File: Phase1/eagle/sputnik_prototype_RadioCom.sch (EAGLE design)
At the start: 56 parts, among them Y1 32MHz

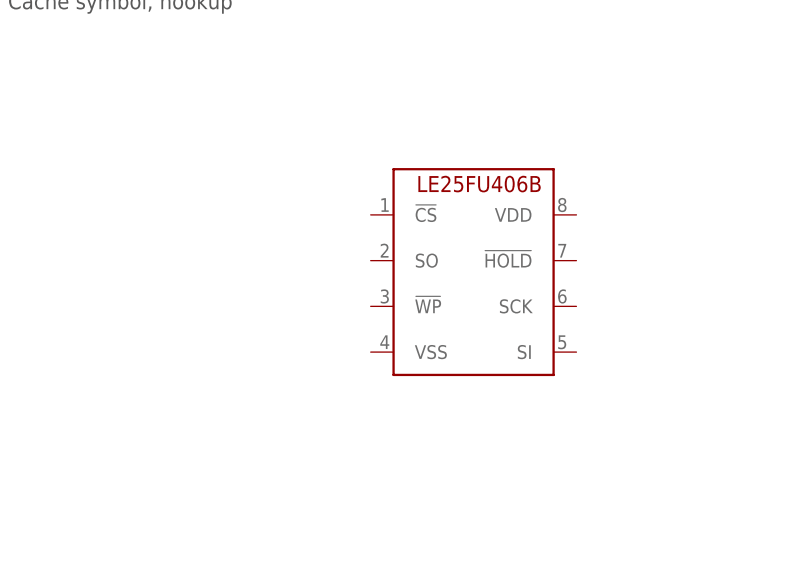
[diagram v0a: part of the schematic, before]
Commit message: Added GPIOs and other updates on SysCon sch. Updated SPI cache footprint
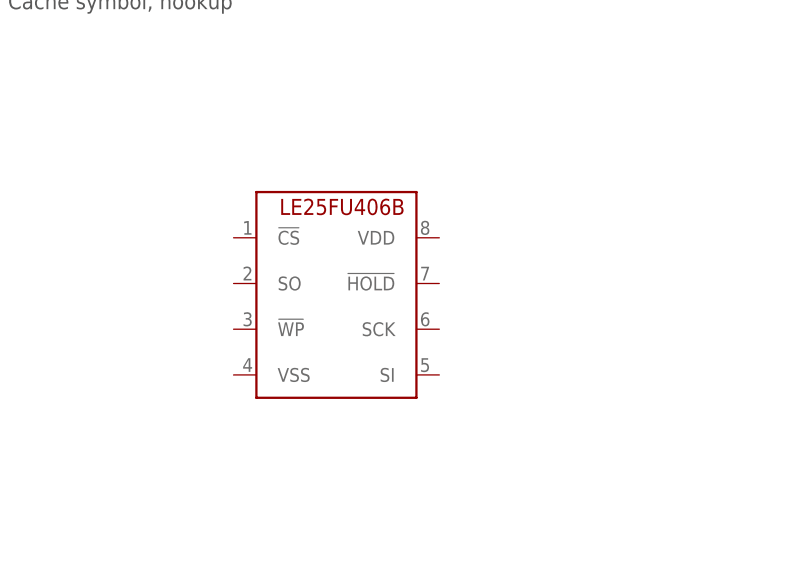
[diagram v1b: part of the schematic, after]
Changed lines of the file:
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@@
 <?xml version="1.0" encoding="utf-8"?>
 <!DOCTYPE eagle SYSTEM "eagle.dtd">
-<eagle version="7.5.0">
+<eagle version="7.4.0">
 <drawing>
 <settings>
@@
 <instance part="U$13" gate="G$1" x="492.76" y="139.7"/>
 <instance part="3.3V2" gate="1" x="419.1" y="142.24" rot="MR0"/>
-<instance part="U$3" gate="G$1" x="337.82" y="127"/>
+<instance part="U$3" gate="G$1" x="322.58" y="124.46"/>
 </instances>
 <busses>
